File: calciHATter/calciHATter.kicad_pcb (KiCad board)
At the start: 2 copper layers, 65 x 56 mm, 30 parts, among them J1 Screw_Terminal_01x02, J2 Jumper, J3 40HAT, U1 MAX31856, U2 CAT24C32

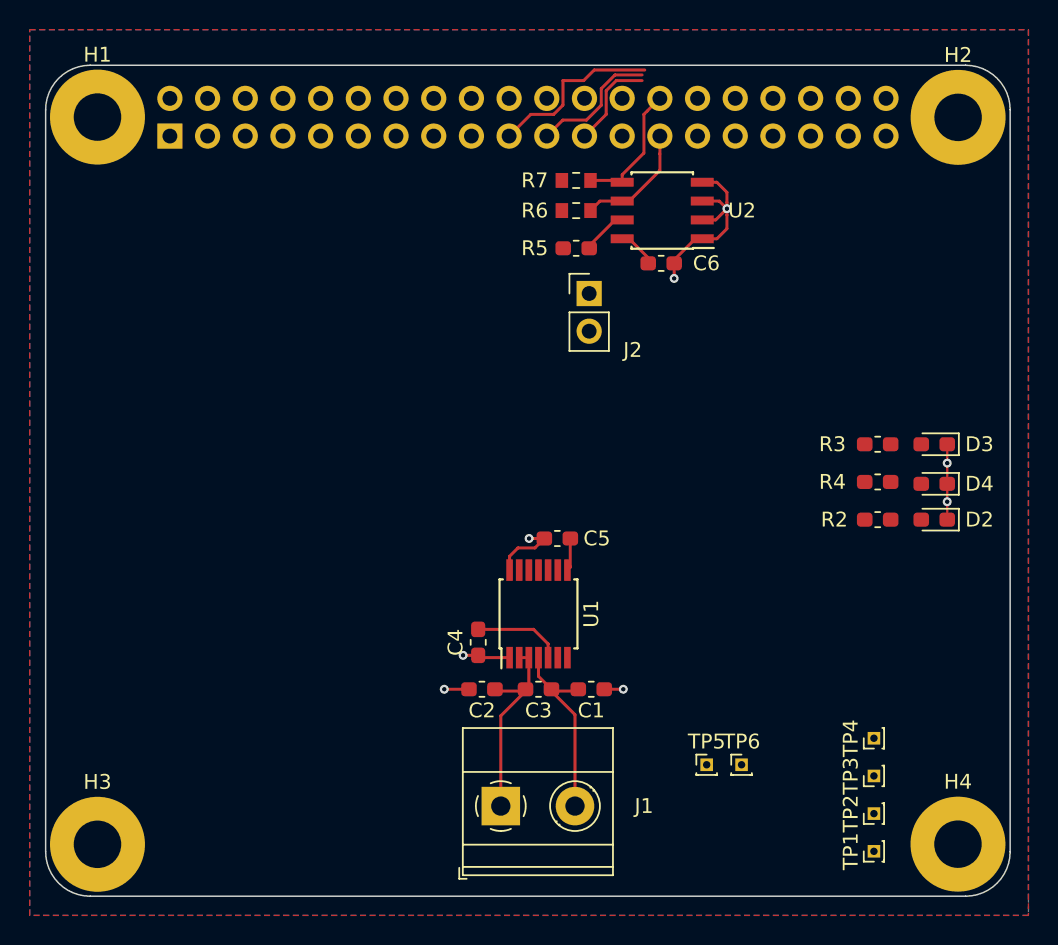
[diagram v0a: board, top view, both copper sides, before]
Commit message: PCB placement to include indicators and toggle switch
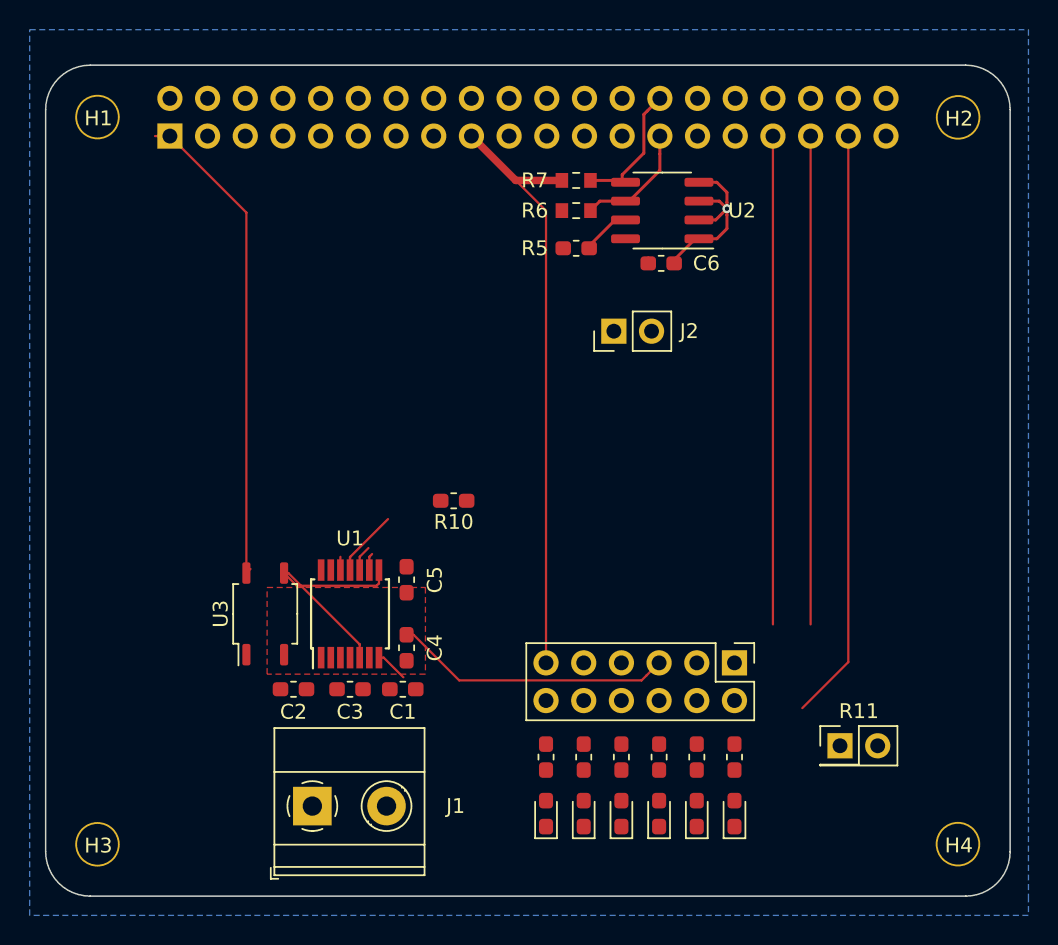
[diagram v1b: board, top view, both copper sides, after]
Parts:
- removed TP1, TP2, TP3, TP4, TP5, TP6: TestPoint, Connector_PinHeader_1.00mm:PinHeader_1x01_P1.00mm_Vertical
- added D1: GREEN, 0603, LED_SMD:LED_0603_1608Metric_Pad1.05x0.95mm_HandSolder, F.Cu at (125.0, 111.3)
- added D5: GREEN, 0603, LED_SMD:LED_0603_1608Metric_Pad1.05x0.95mm_HandSolder, F.Cu at (114.8, 111.3)
- added D6: GREEN, 0603, LED_SMD:LED_0603_1608Metric_Pad1.05x0.95mm_HandSolder, F.Cu at (112.3, 111.3)
- added J4: Conn_02x06_Odd_Even, Connector_PinHeader_2.54mm:PinHeader_2x06_P2.54mm_Vertical, F.Cu at (125.0, 101.1)
- added R1: 1k, 0603, Resistor_SMD:R_0603_1608Metric_Pad1.05x0.95mm_HandSolder, F.Cu at (125.0, 107.4)
- added R10: 10k, 0603, 1%, Resistor_SMD:R_0603_1608Metric_Pad1.05x0.95mm_HandSolder, F.Cu at (106.0, 90.2)
- added R11: R, Connector_PinHeader_2.54mm:PinHeader_2x01_P2.54mm_Vertical, F.Cu at (132.1, 106.7)
- added R8: 1k, 0603, Resistor_SMD:R_0603_1608Metric_Pad1.05x0.95mm_HandSolder, F.Cu at (114.8, 107.4)
- added R9: 1k, 0603, Resistor_SMD:R_0603_1608Metric_Pad1.05x0.95mm_HandSolder, F.Cu at (112.3, 107.4)
- added U3: CPC1125N, Package_SO:SOP-4_3.8x4.1mm_P2.54mm, F.Cu at (93.3, 97.8)
- D2: value LED -> RED, 0603
- D3, D4: value LED -> GREEN, 0603
- H1, H2, H3, H4: value MountingHole_Pad -> MountingHole; footprint MountingHole:MountingHole_3.2mm_M3_Pad -> project_footprints:NPTH_3mm_ID
- J3: value 40HAT -> PI40HAT
- R2, R3, R4: value 1k -> 1k, 0603
- U2: footprint Package_SOIC:SOIC-8_3.9x4.9mm_P1.27mm -> Package_SO:SOIC-8_3.9x4.9mm_P1.27mm
- moved D3 31.0 mm to (119.9, 111.3), turned to 90 degrees
- moved D4 30.6 mm to (117.3, 111.3), turned to 90 degrees
- moved R3 25.7 mm to (119.9, 107.4), turned to 90 degrees
- moved D2 25.5 mm to (122.4, 111.3), turned to 90 degrees
- moved R4 25.3 mm to (117.3, 107.4), turned to 90 degrees
- moved R2 20.1 mm to (122.4, 107.4), turned to 90 degrees
- moved C1 12.7 mm to (102.6, 102.9), turned to 0 degrees
- moved C2 12.7 mm to (95.2, 102.9), turned to 0 degrees
- moved C3 12.7 mm to (99.1, 102.9)
- moved J1 12.7 mm to (96.5, 110.7)
- moved U1 12.7 mm to (99.1, 97.8)
- moved C5 10.5 mm to (102.9, 95.5), turned to 90 degrees
- moved C4 4.84 mm to (102.9, 100.1)
- moved J2 3.04 mm to (116.8, 78.7), turned to 90 degrees
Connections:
- C1 pad 1: GND -> Net-(C1-Pad1)
- C1 pad 2: /TC+ -> GND
- C2 pad 1: /TC- -> GND
- C2 pad 2: GND -> Net-(C2-Pad2)
- C3 pad 1: /TC+ -> Net-(C1-Pad1)
- C3 pad 2: /TC- -> Net-(C2-Pad2)
- C4 pad 2: +3V3 -> /3V3_MAX
- C5 pad 2: +3V3 -> /3V3_MAX
- J1 pad 1: /TC- -> Net-(C2-Pad2)
- J1 pad 2: /TC+ -> Net-(C1-Pad1)
- J3 pad 16: /HBEAT -> Net-(J3-Pad16)
- J3 pad 18: /FAULT -> Net-(J3-Pad18)
- J3 pad 22: /TC_CS -> Net-(J3-Pad22)
- J3 pad 24: /TC_FAULT -> Net-(J3-Pad24)
- J3 pad 26: /TC_~DRDY -> Net-(J3-Pad26)
- J3 pad 33: Net-(J3-Pad33) -> /~TC_CS
- J3 pad 35: Net-(J3-Pad35) -> /~TC_FAULT
- J3 pad 36: Net-(J3-Pad36) -> /FAULT
- J3 pad 37: Net-(J3-Pad37) -> /~TC_DRDY
- J3 pad 38: Net-(J3-Pad38) -> /HBEAT
- J3 pad 40: Net-(J3-Pad40) -> /SOUND
- J3 pad 7: Net-(J3-Pad7) -> /TC_RESET
- R2 pad 1: +3V3 -> Net-(D2-Pad2)
- R2 pad 2: Net-(D2-Pad2) -> Net-(J4-Pad4)
- R3 pad 1: /HBEAT -> Net-(D3-Pad2)
- R3 pad 2: Net-(D3-Pad2) -> Net-(J4-Pad6)
- R4 pad 1: /FAULT -> Net-(D4-Pad2)
- R4 pad 2: Net-(D4-Pad2) -> Net-(J4-Pad8)
- U1 pad 13: /TC_FAULT -> /~TC_FAULT
- U1 pad 2: /TC- -> Net-(C2-Pad2)
- U1 pad 3: /TC- -> Net-(C2-Pad2)
- U1 pad 4: /TC+ -> Net-(C1-Pad1)
- U1 pad 5: +3V3 -> /3V3_MAX
- U1 pad 7: /TC_~DRDY -> /~TC_DRDY
- U1 pad 8: +3V3 -> /3V3_MAX
- U1 pad 9: /TC_CS -> /~TC_CS
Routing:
- net +3V3: track 11.4 -> 80.8 mm
- net /~TC_DRDY: track 0.00 -> 42.0 mm
- net /3V3_MAX: track 0.00 -> 34.5 mm
- net /~TC_CS: track 0.00 -> 34.1 mm
- net /~TC_FAULT: track 0.00 -> 32.9 mm
- net GND: track 29.9 -> 12.9 mm, vias 8 -> 1
- net /TC-: track 13.1 -> 0.00 mm
- net /TC+: track 12.7 -> 0.00 mm
- net /MOSI: track 12.0 -> 0.89 mm
- net /SCLK: track 6.37 -> 1.73 mm
- net /MISO: track 8.79 -> 5.39 mm
- added copper zone on F.Cu, net /3V3_MAX
- removed copper zone on F.Cu, net +3V3
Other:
- net class Default: clearance 0.127 -> 0.254
- rule trace_clearance: 0.127 -> 0.254
- rule trace_min: 0.127 -> 0.13

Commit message: continued layout, some routing & pinout changes
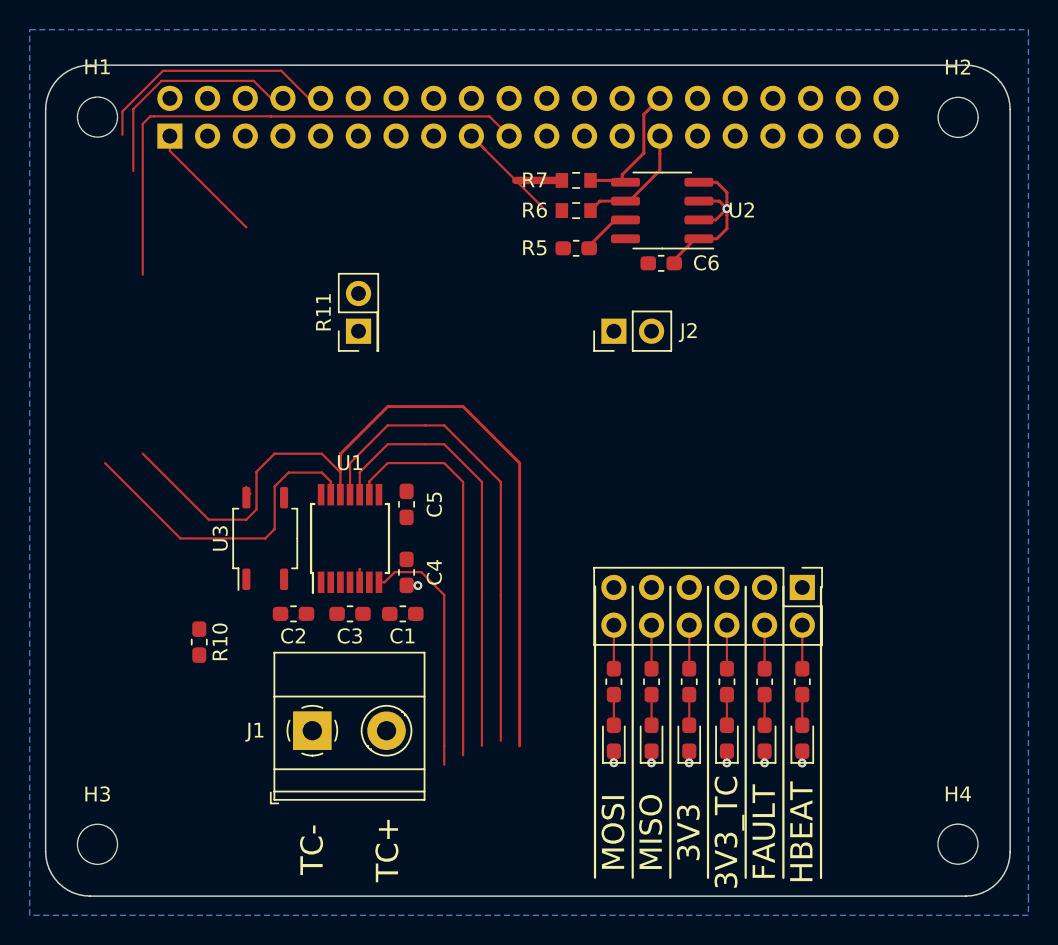
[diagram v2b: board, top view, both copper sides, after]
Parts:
- H1, H2, H3, H4: footprint project_footprints:NPTH_3mm_ID -> MountingHole:MountingHole_2.7mm_M2.5_DIN965
- moved R11 42.8 mm to (99.6, 78.7), turned to 90 degrees
- moved R10 19.6 mm to (88.9, 99.7), turned to 270 degrees
- moved D2 6.83 mm to (127.0, 106.2)
- moved D4 6.83 mm to (121.9, 106.2)
- moved D6 6.83 mm to (116.8, 106.2)
- moved R2 6.83 mm to (127.0, 102.4)
- moved R4 6.83 mm to (121.9, 102.4)
- moved R9 6.83 mm to (116.8, 102.4)
- moved D1 6.83 mm to (129.5, 106.2)
- moved D3 6.83 mm to (124.5, 106.2)
- moved D5 6.83 mm to (119.4, 106.2)
- moved J4 6.83 mm to (129.5, 96.0)
- moved R1 6.83 mm to (129.5, 102.4)
- moved R3 6.83 mm to (124.5, 102.4)
- moved R8 6.83 mm to (119.4, 102.4)
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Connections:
- net Net-(C1-Pad1) renamed /TC+
- net Net-(C2-Pad2) renamed /TC-
- J3 pad 10: Net-(J3-Pad10) -> /TC_RESET
- J3 pad 11: Net-(J3-Pad11) -> /SOUND
- J3 pad 33: /~TC_CS -> Net-(J3-Pad33)
- J3 pad 35: /~TC_FAULT -> Net-(J3-Pad35)
- J3 pad 37: /~TC_DRDY -> Net-(J3-Pad37)
- J3 pad 38: /HBEAT -> /~TC_CS
- J3 pad 40: /SOUND -> /~TC_DRDY
- J3 pad 7: /TC_RESET -> Net-(J3-Pad7)
- J3 pad 8: Net-(J3-Pad8) -> /~TC_FAULT
- J4 pad 1: /MOSI -> /FAULT
- J4 pad 11: +3V3 -> /MOSI
- J4 pad 3: /MISO -> /HBEAT
- J4 pad 7: /FAULT -> +3V3
- J4 pad 9: /HBEAT -> /MISO
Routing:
- net /MOSI: track 0.89 -> 91.7 mm
- net +3V3: track 80.8 -> 22.2 mm
- net /3V3_MAX: track 34.5 -> 0.89 mm
- net /SCLK: track 1.73 -> 29.4 mm
- net /MISO: track 5.39 -> 32.4 mm
- net /~TC_DRDY: track 42.0 -> 17.3 mm
- net /TC_RESET: track 0.00 -> 16.8 mm
- net /~TC_CS: track 34.1 -> 26.7 mm
- net GND: track 12.9 -> 17.6 mm, vias 1 -> 8
- net /~TC_FAULT: track 32.9 -> 37.5 mm
- net Net-(J4-Pad8): track 0.00 -> 2.93 mm
- net Net-(J4-Pad6): track 0.00 -> 2.93 mm
- net Net-(J4-Pad4): track 0.00 -> 2.93 mm
- net Net-(J4-Pad2): track 0.00 -> 2.93 mm
- net Net-(J4-Pad12): track 0.00 -> 2.93 mm
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- removed copper zone on F.Cu, net /3V3_MAX
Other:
- net class Default: clearance 0.254 -> 0.15
- rule trace_clearance: 0.254 -> 0.15
- board text added: "3V3"
- board text added: "3V3_TC"
- board text added: "FAULT"
- board text added: "HBEAT"
- board text added: "MISO"
- board text added: "MOSI"
- board text added: "TC+"
- board text added: "TC-"

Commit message: Finalized pinout, routing. TODO: cleanup+ERC
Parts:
- added R12: 100, Resistor_SMD:R_0603_1608Metric_Pad1.05x0.95mm_HandSolder, F.Cu at (116.5, 102.2)
- added SW1: SW_SPDT, Connector_PinHeader_2.54mm:PinHeader_1x03_P2.54mm_Vertical, F.Cu at (84.0, 95.1)
- C4, C5: value 100n -> 100n, 0603
- D1: value GREEN, 0603 -> RED
- D2: value RED, 0603 -> AMBER
- D3, D4: value GREEN, 0603 -> GREEN
- D5, D6: value GREEN, 0603 -> AMBER
- R1, R2, R3, R4, R8, R9: value 1k, 0603 -> 1k
- R10: value 10k, 0603, 1% -> 10k
- R11: value R -> 100; footprint Connector_PinHeader_2.54mm:PinHeader_2x01_P2.54mm_Vertical -> Resistor_SMD:R_0603_1608Metric_Pad1.05x0.95mm_HandSolder
- moved D1 42.8 mm to (92.1, 85.5), turned to 0 degrees
- moved D2 42.0 mm to (92.1, 82.9), turned to 0 degrees
- moved D6 41.6 mm to (92.1, 72.8), turned to 0 degrees
- moved D3 41.4 mm to (92.1, 80.4), turned to 0 degrees
- moved D5 41.2 mm to (92.1, 75.3), turned to 0 degrees
- moved D4 41.1 mm to (92.1, 77.9), turned to 0 degrees
- moved R10 39.0 mm to (127.6, 95.2), turned to 0 degrees
- moved R1 37.7 mm to (95.9, 85.5), turned to 0 degrees
- moved R2 36.7 mm to (95.9, 82.9), turned to 0 degrees
- moved R9 36.3 mm to (95.9, 72.8), turned to 0 degrees
- moved R3 36.0 mm to (95.9, 80.4), turned to 0 degrees
- moved R8 35.8 mm to (95.9, 75.3), turned to 0 degrees
- moved R4 35.8 mm to (95.9, 77.9), turned to 0 degrees
- moved R11 33.7 mm to (123.9, 102.2), turned to 0 degrees
- moved J4 29.3 mm to (102.2, 85.5), turned to 180 degrees
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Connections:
- C1 pad 1: /TC+ -> Net-(C1-Pad1)
- C2 pad 2: /TC- -> Net-(C2-Pad2)
- C3 pad 1: /TC+ -> Net-(C1-Pad1)
- C3 pad 2: /TC- -> Net-(C2-Pad2)
- J3 pad 10: /TC_RESET -> Net-(J3-Pad10)
- J3 pad 11: /SOUND -> /~TC_FAULT
- J3 pad 13: Net-(J3-Pad13) -> /HBEAT
- J3 pad 3: Net-(J3-Pad3) -> /SOUND
- J3 pad 36: /FAULT -> Net-(J3-Pad36)
- J3 pad 5: Net-(J3-Pad5) -> /TC_RESET
- J3 pad 7: Net-(J3-Pad7) -> /FAULT
- J3 pad 8: /~TC_FAULT -> Net-(J3-Pad8)
- J4 pad 1: /FAULT -> /MOSI
- J4 pad 11: /MOSI -> +3V3
- J4 pad 3: /HBEAT -> /MISO
- J4 pad 7: +3V3 -> /FAULT
- J4 pad 9: /MISO -> /HBEAT
- R11 pad 1: GND -> Net-(C1-Pad1)
- R11 pad 2: /SOUND -> /TC+
- U1 pad 3: /TC- -> Net-(C2-Pad2)
- U1 pad 4: /TC+ -> Net-(C1-Pad1)
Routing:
- net /MISO: track 32.4 -> 84.1 mm
- net /3V3_MAX: track 0.89 -> 44.5 mm
- net /SOUND: track 0.00 -> 34.3 mm
- net /TC_RESET: track 16.8 -> 50.9 mm
- net /~TC_DRDY: track 17.3 -> 45.4 mm
- net /MOSI: track 91.7 -> 66.2 mm
- net +3V3: track 22.2 -> 47.0 mm
- net /SCLK: track 29.4 -> 52.2 mm
- net /~TC_FAULT: track 37.5 -> 59.5 mm
- net /FAULT: track 0.00 -> 17.9 mm
- net /TC-: track 0.32 -> 14.5 mm
- net Net-(J2-Pad1): track 3.11 -> 15.5 mm
- net /HBEAT: track 0.00 -> 10.6 mm
- net /TC+: track 0.00 -> 7.60 mm
- net GND: track 17.6 -> 25.0 mm, vias 8 -> 15
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- added copper zone on F.Cu, net +3V3
- added copper zone on F.Cu, net /3V3_MAX
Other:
- board text added: "OFF"
- board text added: "ON"
- board text added: "SOUND"
- board text added: "calciHATter Rev 1 Marion Anderson F2021"
- board text added: "hey guys, can someone please teach me how to breathe?"

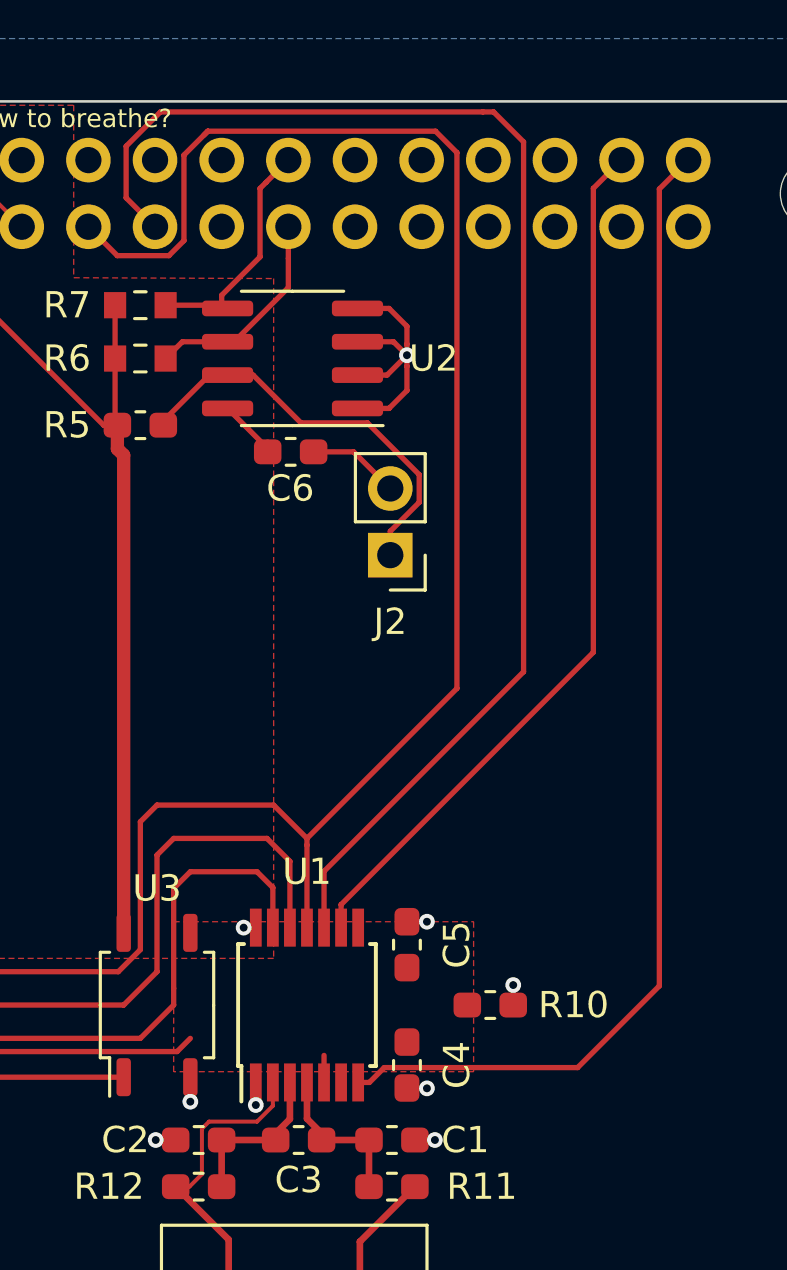
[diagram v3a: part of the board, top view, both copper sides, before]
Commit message: finalized schematic+routing. need easter eggs and footprint checks
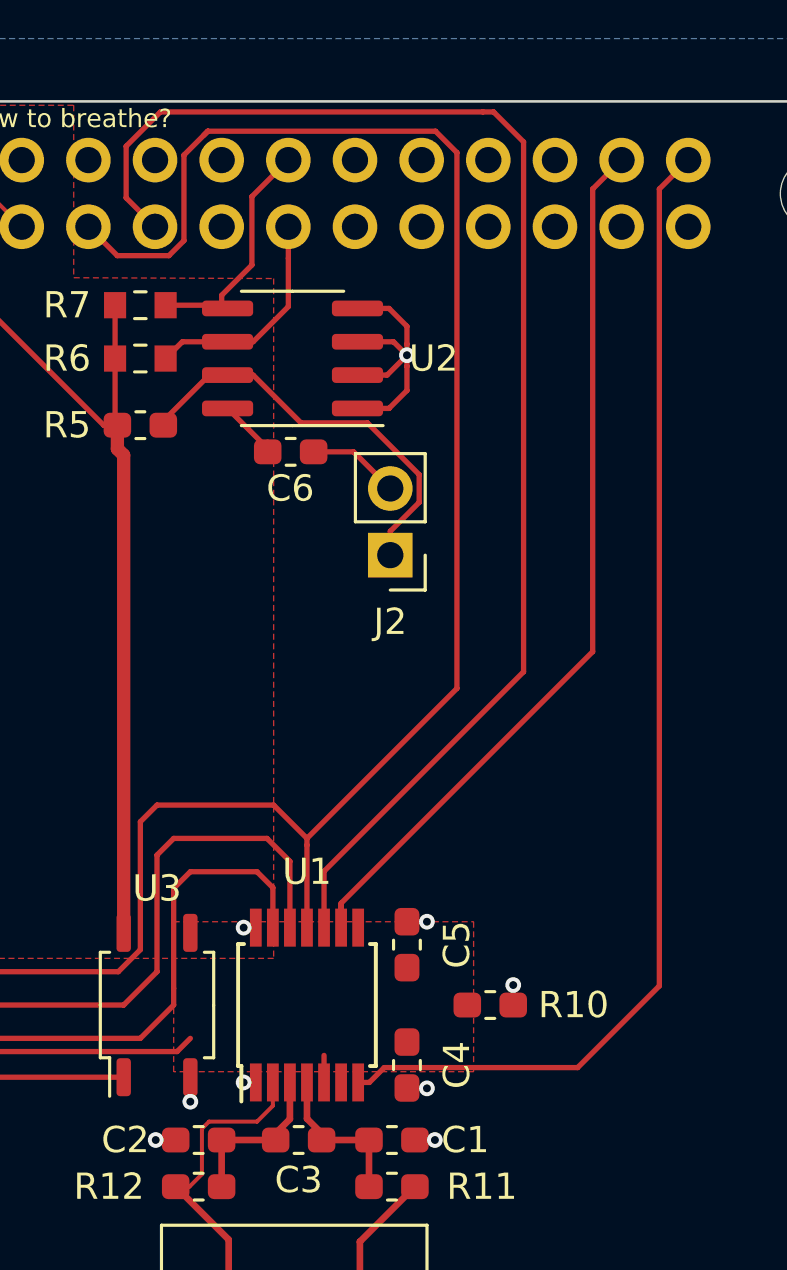
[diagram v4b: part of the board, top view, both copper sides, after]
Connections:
- J3 pad 2: +5C -> Net-(J3-Pad2)
- J3 pad 4: +5C -> Net-(J3-Pad4)
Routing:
- net /~TC_CS: track 33.7 -> 34.6 mm
- net /ID_SD_EEPROM: track 8.59 -> 9.26 mm
- net GND: track 25.0 -> 24.4 mm

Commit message: release calciHATter rev 1 for fab
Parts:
- added G***: LOGO, project_footprints:calcifer, F.Cu at (112.4, 80.6)
- added G***: LOGO, project_footprints:xkcd, B.Cu at (113.7, 91.4)
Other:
- board text added: "A towel is just about the most massively useful thing an interstellar hitchhiker can carry."
- board text added: "It can't be good for the table"
- board text added: "It's not easy being old!"
- board text added: "JLCJLCJLCJLC"
- board text removed: "hey guys, can someone please teach me how to breathe?"
